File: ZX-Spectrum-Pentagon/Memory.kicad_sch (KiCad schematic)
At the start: 10 parts, among them U31 74HC32, U43 74HC257, U44 74HC541, U45 HM628512, U46 74HC574, U47 74HC257, U48 74HC257, U49 74HC257, U51 74HC08

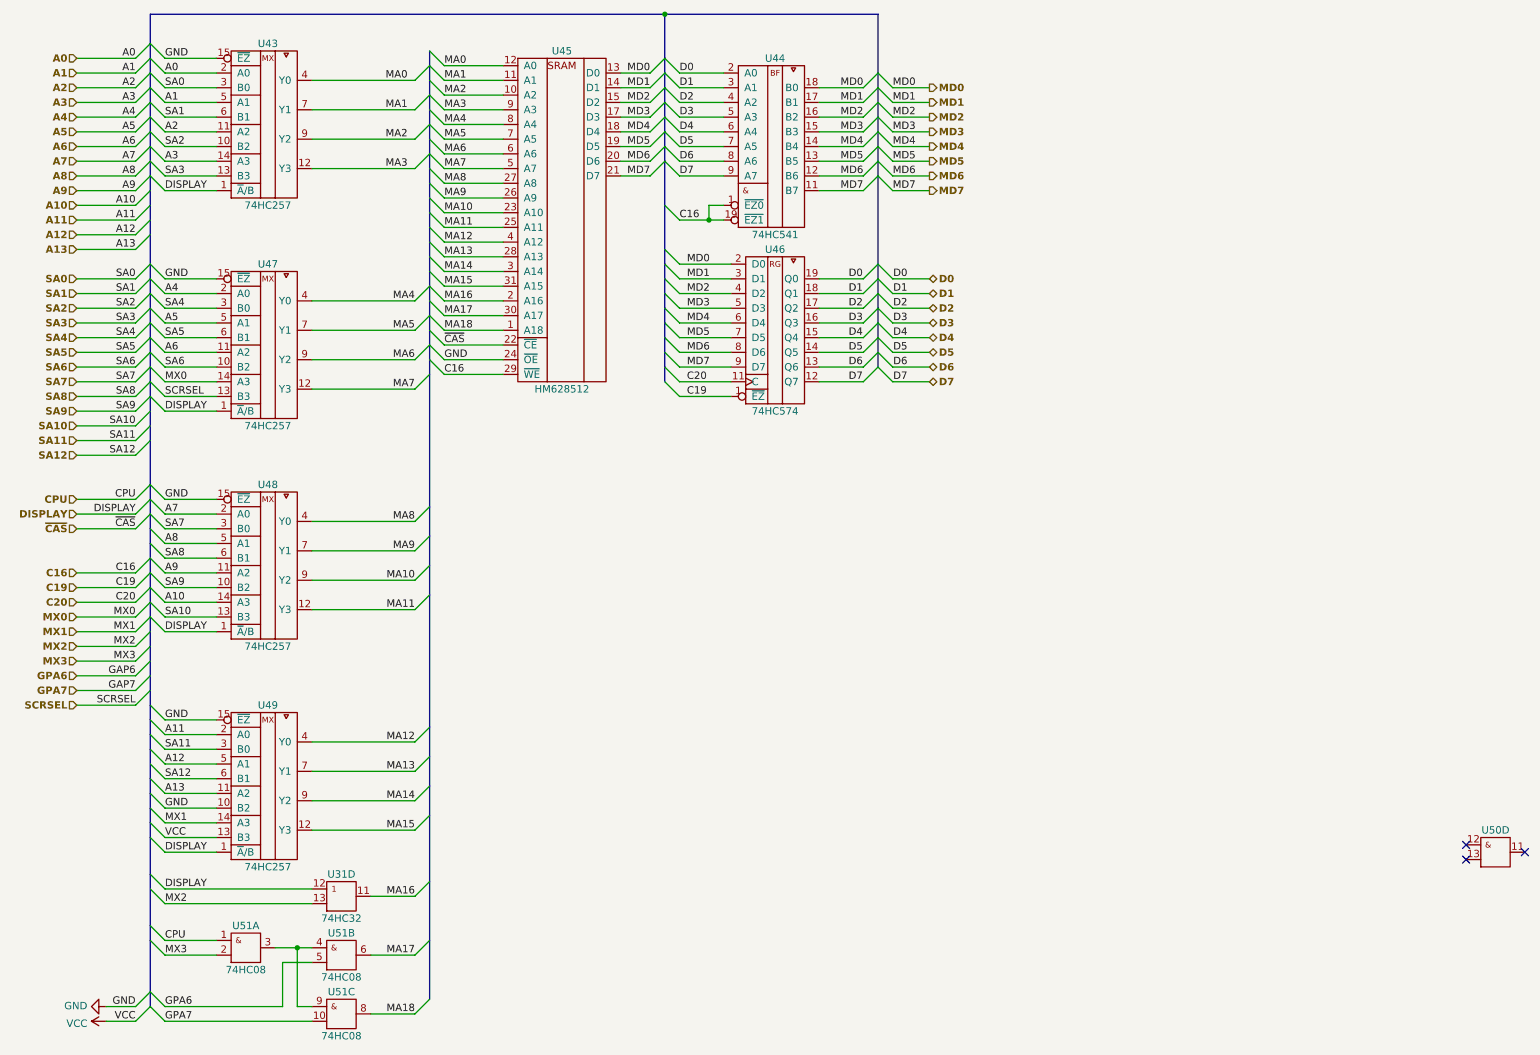
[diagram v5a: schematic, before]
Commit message: delete unuser labels fix problem with units
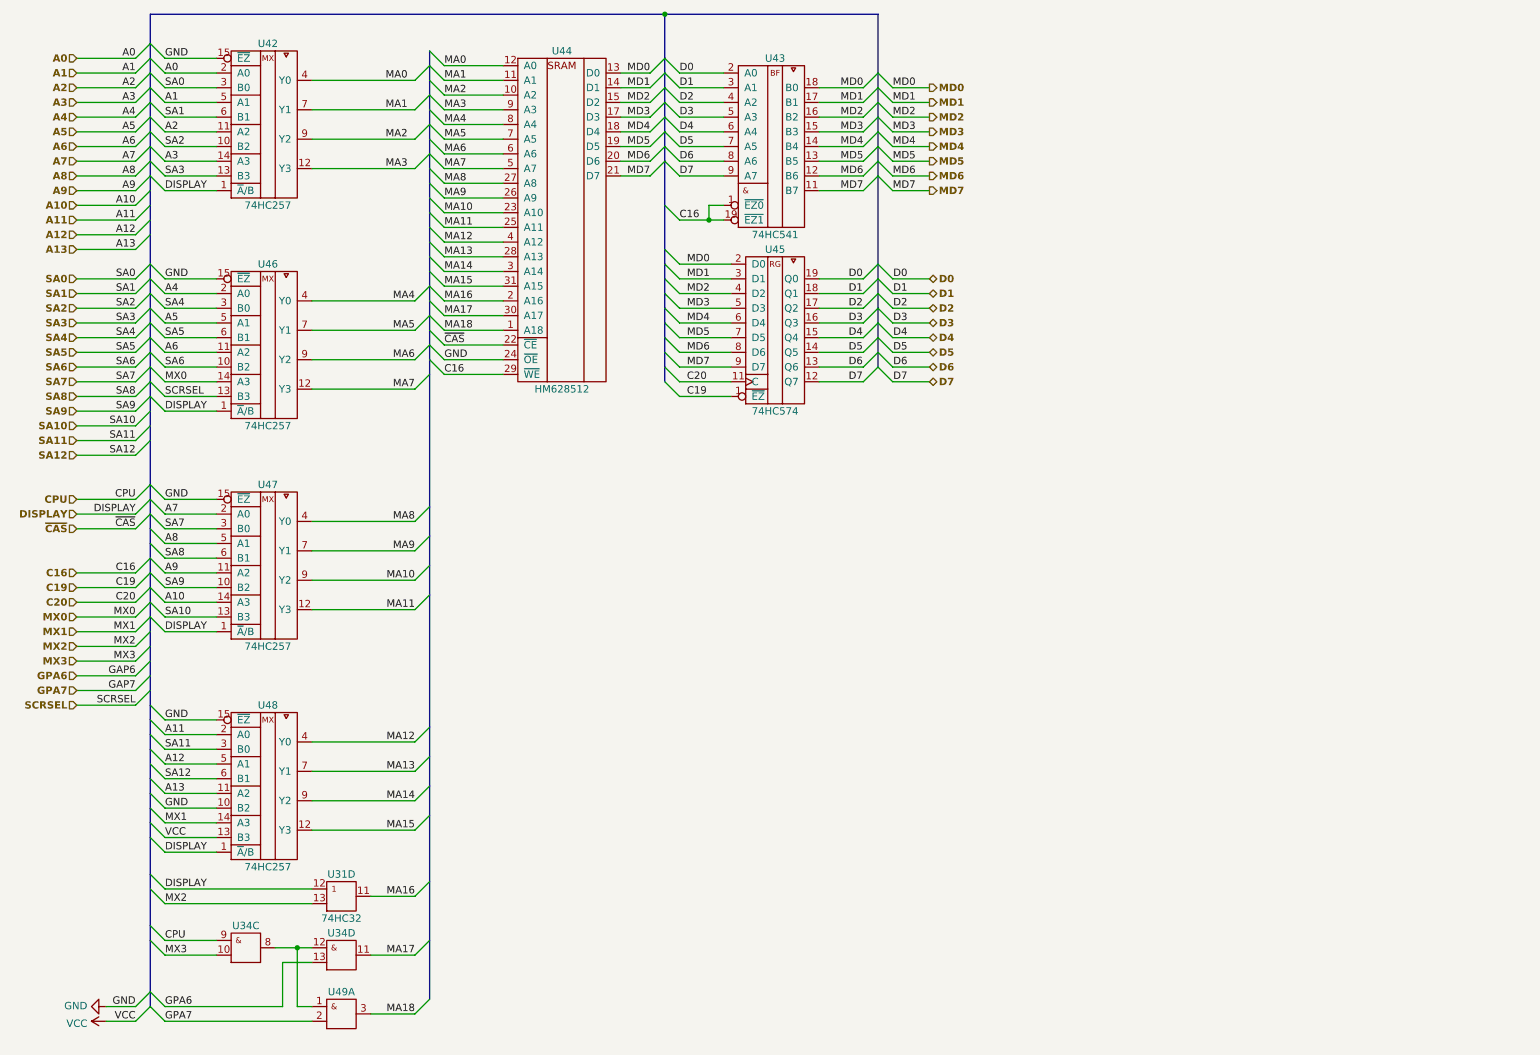
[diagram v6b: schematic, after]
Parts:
- removed U50: ~, symbol 74IEC:74HC08
- U34, U49: renamed from U51; value 74HC08 -> (none); footprint Package_DIP:DIP-14_W7.62mm -> (none)
- renumbered U43 to U42, U44 to U43, U45 to U44, U46 to U45, U47 to U46, U48 to U47, U49 to U48
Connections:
- net CPU: now also U34.9 (A); no longer U34.1 (A)
- net GPA6: now also U34.13 (B); no longer U34.5 (B)
- net GPA7: now also U49.2 (B); no longer U49.10 (B)
- net MA17: now also U34.11 (~{Y}); no longer U34.6 (~{Y})
- net MA18: now also U49.3 (~{Y}); no longer U49.8 (~{Y})
- net MX3: now also U34.10 (B); no longer U34.2 (B)
- new net: U34.12 (A), U34.8 (~{Y}), U49.1 (A)
- no-connect marks 3 -> 0
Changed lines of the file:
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@@
   (junction (at 127 13.97) (diameter 0) (color 0 0 0 0)
   )
-  (no_connect (at 265.43 160.02))
-  (no_connect (at 275.59 158.75))
-  (no_connect (at 265.43 157.48))
   (bus_entry (at 38.1 135.89) (size 2.54 2.54)
     (stroke (width 0) (type default) (color 0 0 0 0))
@@
   (symbol (lib_id "GenericSRAM:HM628512") (at 109.22 49.53 0) (unit 1)
     (in_bom yes) (on_board yes)
-    (property "Reference" "U45" (id 0) (at 109.22 20.32 0))
+    (property "Reference" "U44" (id 0) (at 109.22 20.32 0))
     (property "Value" "HM628512" (id 1) (at 109.22 78.74 0))
     (property "Footprint" "Package_DIP:DIP-32_W15.24mm" (id 2) (at 109.22 20.32 0)
@@
   (symbol (lib_id "74IEC:74HC541") (at 146.05 35.56 0) (unit 1)
     (in_bom yes) (on_board yes)
-    (property "Reference" "U44" (id 0) (at 146.05 21.59 0))
+    (property "Reference" "U43" (id 0) (at 146.05 21.59 0))
     (property "Value" "74HC541" (id 1) (at 146.05 52.07 0))
     (property "Footprint" "Package_DIP:DIP-20_W7.62mm" (id 2) (at 146.05 21.59 0)
@@
   (symbol (lib_id "74IEC:74HC257") (at 58.42 33.02 0) (unit 1)
     (in_bom yes) (on_board yes)
-    (property "Reference" "U43" (id 0) (at 58.42 19.05 0))
+    (property "Reference" "U42" (id 0) (at 58.42 19.05 0))
     (property "Value" "74HC257" (id 1) (at 58.42 46.99 0))
     (property "Footprint" "Package_DIP:DIP-16_W7.62mm" (id 2) (at 72.39 31.75 0)
@@
   (symbol (lib_id "74IEC:74HC257") (at 58.42 71.12 0) (unit 1)
     (in_bom yes) (on_board yes)
-    (property "Reference" "U47" (id 0) (at 58.42 57.15 0))
+    (property "Reference" "U46" (id 0) (at 58.42 57.15 0))
     (property "Value" "74HC257" (id 1) (at 58.42 85.09 0))
     (property "Footprint" "Package_DIP:DIP-16_W7.62mm" (id 2) (at 72.39 69.85 0)
@@
   (symbol (lib_id "74IEC:74HC257") (at 58.42 109.22 0) (unit 1)
     (in_bom yes) (on_board yes)
-    (property "Reference" "U48" (id 0) (at 58.42 95.25 0))
+    (property "Reference" "U47" (id 0) (at 58.42 95.25 0))
     (property "Value" "74HC257" (id 1) (at 58.42 123.19 0))
     (property "Footprint" "Package_DIP:DIP-16_W7.62mm" (id 2) (at 72.39 107.95 0)
@@
   (symbol (lib_id "74IEC:74HC257") (at 58.42 147.32 0) (unit 1)
     (in_bom yes) (on_board yes)
-    (property "Reference" "U49" (id 0) (at 58.42 133.35 0))
+    (property "Reference" "U48" (id 0) (at 58.42 133.35 0))
     (property "Value" "74HC257" (id 1) (at 58.42 161.29 0))
     (property "Footprint" "Package_DIP:DIP-16_W7.62mm" (id 2) (at 72.39 146.05 0)
@@
   (symbol (lib_id "74IEC:74HC574") (at 146.05 68.58 0) (unit 1)
     (in_bom yes) (on_board yes)
-    (property "Reference" "U46" (id 0) (at 146.05 54.61 0))
+    (property "Reference" "U45" (id 0) (at 146.05 54.61 0))
     (property "Value" "74HC574" (id 1) (at 146.05 82.55 0))
     (property "Footprint" "Package_DIP:DIP-20_W7.62mm" (id 2) (at 146.05 76.2 0)
@@
     (pin "9")
   )
-  (symbol (lib_id "74IEC:74HC08") (at 71.12 176.53 0) (unit 2)
+  (symbol (lib_id "74IEC:74HC08") (at 71.12 176.53 0) (unit 4)
     (in_bom yes) (on_board yes)
-    (property "Reference" "U51" (id 0) (at 71.12 172.72 0))
-    (property "Value" "74HC08" (id 1) (at 71.12 180.34 0))
-    (property "Footprint" "Package_DIP:DIP-14_W7.62mm" (id 2) (at 71.12 184.15 0)
+    (property "Reference" "U34" (id 0) (at 71.12 172.72 0))
+    (property "Value" "" (id 1) (at 71.12 180.34 0))
+    (property "Footprint" "" (id 2) (at 71.12 184.15 0)
       (effects (font (size 1.27 1.27)) hide)
     )
@@
     (pin "13")
   )
-  (symbol (lib_id "74IEC:74HC08") (at 71.12 186.69 0) (unit 3)
+  (symbol (lib_id "74IEC:74HC08") (at 71.12 186.69 0) (unit 1)
     (in_bom yes) (on_board yes)
-    (property "Reference" "U51" (id 0) (at 71.12 182.88 0))
-    (property "Value" "74HC08" (id 1) (at 71.12 190.5 0))
-    (property "Footprint" "Package_DIP:DIP-14_W7.62mm" (id 2) (at 71.12 194.31 0)
+    (property "Reference" "U49" (id 0) (at 71.12 182.88 0))
+    (property "Value" "" (id 1) (at 71.12 190.5 0))
+    (property "Footprint" "" (id 2) (at 71.12 194.31 0)
       (effects (font (size 1.27 1.27)) hide)
     )
@@
     (pin "13")
   )
-  (symbol (lib_id "74IEC:74HC08") (at 54.61 175.26 0) (unit 1)
+  (symbol (lib_id "74IEC:74HC08") (at 54.61 175.26 0) (unit 3)
     (in_bom yes) (on_board yes)
-    (property "Reference" "U51" (id 0) (at 54.61 171.45 0))
-    (property "Value" "74HC08" (id 1) (at 54.61 179.07 0))
-    (property "Footprint" "Package_DIP:DIP-14_W7.62mm" (id 2) (at 54.61 182.88 0)
+    (property "Reference" "U34" (id 0) (at 54.61 171.45 0))
+    (property "Value" "" (id 1) (at 54.61 179.07 0))
+    (property "Footprint" "" (id 2) (at 54.61 182.88 0)
       (effects (font (size 1.27 1.27)) hide)
     )
@@
       (effects (font (size 1.27 1.27)) hide)
     )
-    (pin "14")
-    (pin "7")
-    (pin "1")
-    (pin "2")
-    (pin "3")
-    (pin "4")
-    (pin "5")
-    (pin "6")
-    (pin "10")
-    (pin "8")
-    (pin "9")
-    (pin "11")
-    (pin "12")
-    (pin "13")
-  )
-  (symbol (lib_id "74IEC:74HC08") (at 270.51 158.75 0) (unit 4)
-    (in_bom yes) (on_board no)
-    (property "Reference" "U50" (id 0) (at 270.51 154.94 0))
-    (property "Value" "~" (id 1) (at 270.51 162.56 0))
-    (property "Footprint" "" (id 2) (at 270.51 166.37 0)
-      (effects (font (size 1.27 1.27)) hide)
-    )
-    (property "Datasheet" "https://www.ti.com/lit/ug/scyd013b/scyd013b.pdf" (id 3) (at 270.51 154.94 0)
-      (effects (font (size 1.27 1.27)) hide)
-    )

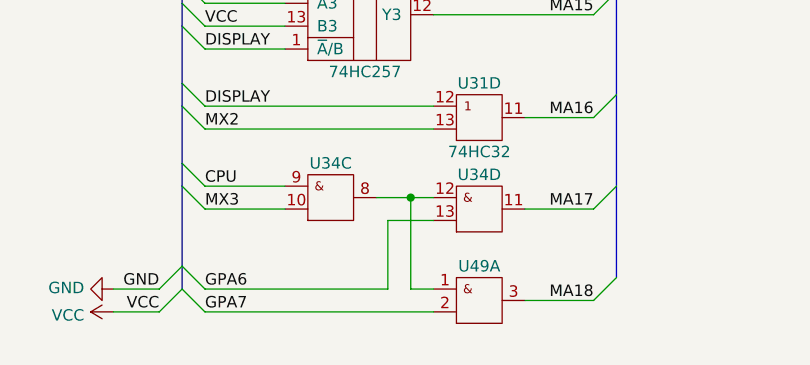
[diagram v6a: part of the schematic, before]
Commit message: chsnge some signals Make a track between CPU and buffers
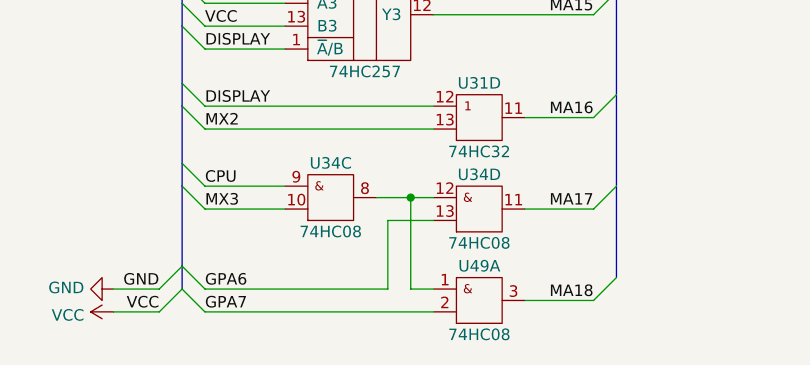
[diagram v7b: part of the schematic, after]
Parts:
- U34, U49: value (none) -> 74HC08; footprint (none) -> Package_DIP:DIP-14_W7.62mm
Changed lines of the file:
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@@
     (in_bom yes) (on_board yes)
     (property "Reference" "U34" (id 0) (at 71.12 172.72 0))
-    (property "Value" "" (id 1) (at 71.12 180.34 0))
-    (property "Footprint" "" (id 2) (at 71.12 184.15 0)
+    (property "Value" "74HC08" (id 1) (at 71.12 180.34 0))
+    (property "Footprint" "Package_DIP:DIP-14_W7.62mm" (id 2) (at 71.12 184.15 0)
       (effects (font (size 1.27 1.27)) hide)
     )
@@
     (in_bom yes) (on_board yes)
     (property "Reference" "U49" (id 0) (at 71.12 182.88 0))
-    (property "Value" "" (id 1) (at 71.12 190.5 0))
-    (property "Footprint" "" (id 2) (at 71.12 194.31 0)
+    (property "Value" "74HC08" (id 1) (at 71.12 190.5 0))
+    (property "Footprint" "Package_DIP:DIP-14_W7.62mm" (id 2) (at 71.12 194.31 0)
       (effects (font (size 1.27 1.27)) hide)
     )
@@
     (in_bom yes) (on_board yes)
     (property "Reference" "U34" (id 0) (at 54.61 171.45 0))
-    (property "Value" "" (id 1) (at 54.61 179.07 0))
-    (property "Footprint" "" (id 2) (at 54.61 182.88 0)
+    (property "Value" "74HC08" (id 1) (at 54.61 179.07 0))
+    (property "Footprint" "Package_DIP:DIP-14_W7.62mm" (id 2) (at 54.61 182.88 0)
       (effects (font (size 1.27 1.27)) hide)
     )

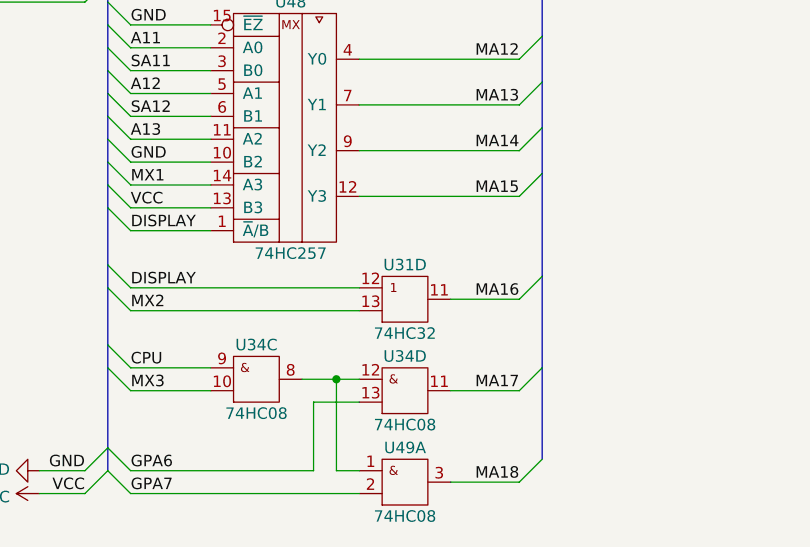
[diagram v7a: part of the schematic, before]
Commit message: reconnect U31 trace U31 tracing
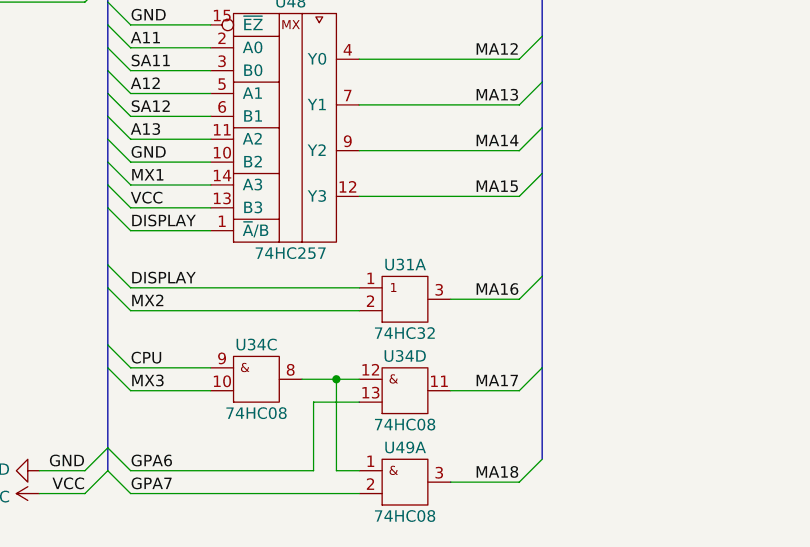
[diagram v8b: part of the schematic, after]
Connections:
- net DISPLAY: now also U31.1 (A); no longer U31.12 (A)
- net MA16: now also U31.3 (Y); no longer U31.11 (Y)
- net MX2: now also U31.2 (B); no longer U31.13 (B)
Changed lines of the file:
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@@
     (pin "1")
   )
-  (symbol (lib_id "74IEC:74HC32") (at 71.12 166.37 0) (unit 4)
+  (symbol (lib_id "74IEC:74HC32") (at 71.12 166.37 0) (unit 1)
     (in_bom yes) (on_board yes)
     (property "Reference" "U31" (id 0) (at 71.12 162.56 0))
